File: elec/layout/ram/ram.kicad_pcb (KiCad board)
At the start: 2 copper layers, 40 x 40 mm, 56 parts, among them U1 _NXP_Semicon_MIMX8MM6CVTKZAA

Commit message: Building! started on layout
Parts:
- removed C37, C48: 10µF ±20% 6.3V X5R, lcsc:C0402
- removed C38, C39, C40, C41, C42, C43, C50, C51, C52, C53, C54: 1µF ±20% 6.3V X5R, lcsc:C0201
- removed C44, C46, C47, C55: 220nF ±20% 6.3V X5R, lcsc:C0201
- removed C45: 2.2µF ±20% 6.3V X5R, lcsc:C0402
- removed C49: 4.7µF ±20% 10V X5R, lcsc:C0402
- C1: value 2.2µF ±20% 6.3V X5R -> 10µF ±20% 6.3V X5R; footprint lcsc:C0201 -> lcsc:C0402; moved to B.Cu
- C10, C11, C13, C16, C17, C24, C26, C27, C28, C30: moved to B.Cu
- C12, C14, C32, C33, C34, C35, C4, C5, C6, C7, C8, C9: value 1µF ±20% 6.3V X5R -> 220nF ±20% 6.3V X5R; moved to B.Cu
- C15, C2, C3, C36: value 10µF ±20% 6.3V X5R -> 220nF ±20% 6.3V X5R; footprint lcsc:C0402 -> lcsc:C0201; moved to B.Cu
- C18, C19, C20, C21, C22, C23, C29: value 220nF ±20% 6.3V X5R -> 10µF ±20% 6.3V X5R; footprint lcsc:C0201 -> lcsc:C0402; moved to B.Cu
- C25: value 4.7µF ±20% 10V X5R -> 10µF ±20% 6.3V X5R; moved to B.Cu
- C31: value 1µF ±20% 6.3V X5R -> 10µF ±20% 6.3V X5R; footprint lcsc:C0201 -> lcsc:C0402; moved to B.Cu
- U1: value _NXP_Semicon_MIMX8MM6CVTKZAA -> _SK_HYNIX_H9HCNNNBKUMLXR_NEE; footprint lcsc:BGA-486_L14.0-W14.0-P0.50-TL_NXP_MIMX8MMXDVTLZXA -> lcsc:FBGA-200_L15.0-W10.0-BL_H9HCNNNBKUMLXR
- moved C13 188.4 mm to (161.6, 96.9)
- moved C12 187.3 mm to (161.6, 94.8)
- moved C6 186.4 mm to (158.8, 97.7), turned to 180 degrees
- moved C11 186.2 mm to (161.6, 92.6)
- moved C5 185.4 mm to (158.8, 95.8), turned to 180 degrees
- moved C1 185.2 mm to (161.6, 90.5), turned to 180 degrees
- moved C4 184.4 mm to (158.8, 93.8), turned to 180 degrees
- moved C3 183.5 mm to (158.8, 91.9), turned to 180 degrees
- moved C2 182.5 mm to (158.8, 90.0), turned to 180 degrees
- moved C20 181.9 mm to (152.7, 98.8), turned to 180 degrees
- moved C27 181.5 mm to (152.7, 98.1), turned to 180 degrees
- moved C24 179.8 mm to (152.4, 95.4), turned to 90 degrees
- moved C26 178.1 mm to (152.4, 92.2), turned to -90 degrees
- moved C35 177.0 mm to (152.7, 89.4), turned to 180 degrees
- moved U1 176.4 mm to (149.5, 93.8)
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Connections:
- net dram_ac00 renamed signal-16
- net dram_ac03 renamed signal-14
- net dram_ac10 renamed signal-49
- net dram_ac23 renamed signal-25
- net dram_ac24 renamed signal-55
- net dram_ac32 renamed signal-28
- net dram_alert_n renamed signal-12
- net dram_dq00 renamed zq0
- net dram_dq07 renamed signal-53
- net dram_dq08 renamed signal-3
- net dram_dq11 renamed signal-0
- net dram_dq15 renamed signal-33
- net dram_dq17 renamed signal-5
- net dram_dq20 renamed signal-9
- net dram_dqs0_n renamed signal-34
- net dram_zn renamed signal-59
- net i2c1_scl renamed signal-24
- net i2c1_sda renamed signal-36
- net i2c2_scl renamed signal-57
- net i2c3_scl renamed signal-11
- net mipi_dsi_clk_p renamed signal-22
- net mipi_dsi_d0_p renamed signal-26
- net vdd_dram_pll_0p8 renamed ck_cb
- C1 pad 1: *BC98.processor-net-1 -> NVCC_DRAM_1V1
- C10 pad 1: NVCC_ENET -> NVCC_DRAM_1V1
- C11 pad 1: NVCC_SD2 -> NVCC_DRAM_1V1
- C12 pad 1: *BC98.processor-net-0 -> NVCC_DRAM_1V1
- C13 pad 1: VDDA_1V8 -> NVCC_DRAM_1V1
- C14 pad 1: VDDA_1V8 -> NVCC_DRAM_1V1
- C15 pad 1: VDDA_1V8 -> NVCC_DRAM_1V1
- C16 pad 1: VDDA_1V8 -> NVCC_DRAM_1V1
- C17 pad 1: VDDA_1V8 -> NVCC_DRAM_1V1
- C18 pad 1: VDDA_1V8 -> NVCC_DRAM_1V1
- C19 pad 1: VDDA_1V8 -> NVCC_DRAM_1V1
- C20 pad 1: VDDA_1V8 -> NVCC_DRAM_1V1
- C21 pad 1: VDDA_1V8 -> NVCC_DRAM_1V1
- C22 pad 1: VDDA_1V8 -> NVCC_DRAM_1V1
- C23 pad 1: VDDA_1V8 -> NVCC_DRAM_1V1
- C24 pad 1: VDDA_1V8 -> NVCC_DRAM_1V1
- C25 pad 1: VDD_3V3 -> VDD_1V8
- C26 pad 1: VDD_3V3 -> VDD_1V8
- C27 pad 1: VDD_3V3 -> VDD_1V8
- C28 pad 1: VDD_3V3 -> VDD_1V8
- C29 pad 1: VDD_3V3 -> VDD_1V8
- C30 pad 1: VDD_ARM_0V9 -> VDD_1V8
- C31 pad 1: VDD_ARM_0V9 -> VDD_1V8
- C32 pad 1: VDD_ARM_0V9 -> VDD_1V8
- C33 pad 1: VDD_ARM_0V9 -> VDD_1V8
- C34 pad 1: VDD_ARM_0V9 -> VDD_1V8
- C35 pad 1: VDD_ARM_0V9 -> VDD_1V8
- C36 pad 1: VDD_DRAM_0V9 -> VDD_1V8
- U1 pad A1: GND -> *5FE8.RAM.RAM-net-0
- U1 pad A10: mipi_dsi_d1_n -> GND
- U1 pad A11: mipi_dsi_clk_n -> *5FE8.RAM.RAM-net-0
- U1 pad A12: mipi_dsi_d2_n -> *5FE8.RAM.RAM-net-0
- U1 pad A2: dram_dqs0_p -> *5FE8.RAM.RAM-net-0
- U1 pad A3: dram_dq06 -> GND
- U1 pad A4: dram_dm0 -> NVCC_DRAM_1V1
- U1 pad A8: ecspi2_miso -> *5FE8.RAM.RAM-net-1
- U1 pad A9: mipi_dsi_d0_n -> NVCC_DRAM_1V1
- U1 pad AA1: dram_dqs2_p -> *5FE8.RAM.RAM-net-0
- U1 pad AA10: GND -> NVCC_DRAM_1V1
- U1 pad AA9: GND -> signal-42
- U1 pad AB1: dram_dm2 -> *5FE8.RAM.RAM-net-0
- U1 pad AB10: gpio1_io12 -> GND
- U1 pad AB2: dram_dq16 -> *5FE8.RAM.RAM-net-0
- U1 pad AB4: dram_ac20 -> NVCC_DRAM_1V1
- U1 pad AB5: dram_ac21 -> GND
- U1 pad AB9: gpio1_io15 -> NVCC_DRAM_1V1
- U1 pad B1: dram_dq05 -> *5FE8.RAM.RAM-net-0
- U1 pad B10: mipi_dsi_d1_p -> NVCC_DRAM_1V1
- U1 pad B12: mipi_dsi_d2_p -> *5FE8.RAM.RAM-net-0
- U1 pad B3: GND -> NVCC_DRAM_1V1
- U1 pad B5: dram_dq01 -> NVCC_DRAM_1V1
- U1 pad B8: ecspi2_mosi -> NVCC_DRAM_1V1
- U1 pad C1: dram_dq04 -> GND
- U1 pad C10: GND -> signal-38
- U1 pad C2: GND -> signal-4
- U1 pad C9: GND -> signal-39
- U1 pad D1: dram_dq03 -> NVCC_DRAM_1V1
- U1 pad D2: dram_dq02 -> GND
- U1 pad D5: dram_ac11 -> NVCC_DRAM_1V1
- U1 pad D9: i2c2_sda -> GND
- U1 pad E1: dram_dq14 -> GND
- U1 pad E3: GND -> signal-40
- U1 pad F1: dram_dm1 -> VDD_1V8
- U1 pad F10: i2c3_sda -> NVCC_DRAM_1V1
- U1 pad F3: GND -> NVCC_DRAM_1V1
- U1 pad F5: dram_ac01 -> NVCC_DRAM_1V1
- U1 pad G1: dram_dqs1_p -> GND
- U1 pad G2: dram_dq09 -> NVCC_DRAM_1V1
- U1 pad G9: GND -> VDD_1V8
- U1 pad H1: dram_dqs1_n -> NVCC_DRAM_1V1
- U1 pad H10: VDD_3V3 -> signal-7
- U1 pad H2: GND -> signal-31
- U1 pad J1: dram_dq10 -> GND
- U1 pad J10: VDD_DRAM_0V9 -> GND
- U1 pad J11: VDDA_1V8 -> signal-43
- U1 pad J12: VDDA_1V8 -> GND
- U1 pad J5: dram_ac07 -> *5FE8.RAM.RAM-net-1
- U1 pad K1: dram_dq13 -> NVCC_DRAM_1V1
- U1 pad K12: VDD_DRAM_0V9 -> NVCC_DRAM_1V1
- U1 pad K2: dram_dq12 -> GND
- U1 pad K3: GND -> NVCC_DRAM_1V1
- U1 pad K4: dram_ac02 -> GND
- U1 pad K5: dram_ac14 -> *5FE8.RAM.RAM-net-1
- U1 pad K8: NVCC_DRAM_1V1 -> *5FE8.RAM.RAM-net-1
- U1 pad K9: NVCC_DRAM_1V1 -> GND
- U1 pad N1: dram_ac26 -> NVCC_DRAM_1V1
- U1 pad N10: VDD_DRAM_0V9 -> NVCC_DRAM_1V1
- U1 pad N11: VDD_DRAM_0V9 -> GND
- U1 pad N12: GND -> NVCC_DRAM_1V1
- U1 pad N2: dram_ac19 -> GND
- U1 pad N3: GND -> NVCC_DRAM_1V1
- U1 pad N4: dram_ac12 -> GND
- U1 pad N5: dram_ac13 -> *5FE8.RAM.RAM-net-1
- U1 pad N8: NVCC_DRAM_1V1 -> *5FE8.RAM.RAM-net-1
- U1 pad N9: NVCC_DRAM_1V1 -> GND
- U1 pad P1: dram_vref -> GND
- U1 pad P12: VDD_DRAM_0V9 -> GND
- U1 pad P5: VDD_DRAM_0V9 -> *5FE8.RAM.RAM-net-1
- U1 pad R1: dram_reset_n -> NVCC_DRAM_1V1
- U1 pad R10: VDD_DRAM_0V9 -> signal-50
- U1 pad R11: VDD_DRAM_0V9 -> signal-58
- U1 pad R12: GND -> NVCC_DRAM_1V1
- U1 pad R3: GND -> *5FE8.RAM.RAM-net-1
- U1 pad R5: dram_ac33 -> NVCC_DRAM_1V1
- U1 pad R9: NVCC_DRAM_1V1 -> signal-52
- U1 pad T1: dram_ac234 -> GND
- U1 pad T2: dram_ac35 -> NVCC_DRAM_1V1
- U1 pad T9: NVCC_DRAM_1V1 -> VDD_1V8
- U1 pad U1: dram_ac25 -> VDD_1V8
- U1 pad U10: VDD_DRAM_0V9 -> NVCC_DRAM_1V1
- U1 pad U11: VDD_DRAM_0V9 -> signal-37
- U1 pad U12: GND -> VDD_1V8
- U1 pad U9: NVCC_DRAM_1V1 -> signal-32
- U1 pad V1: dram_dq21 -> GND
- U1 pad V12: VDD_DRAM_0V9 -> GND
- U1 pad V3: GND -> signal-18
- U1 pad V5: dram_ac36 -> GND
- U1 pad V8: NVCC_DRAM_1V1 -> GND
- U1 pad V9: NVCC_DRAM_1V1 -> signal-47
- U1 pad W1: dram_dq18 -> NVCC_DRAM_1V1
- U1 pad W10: VDD_DRAM_0V9 -> signal-15
- U1 pad W11: VDD_DRAM_0V9 -> GND
- U1 pad W12: VDDA_1V8 -> NVCC_DRAM_1V1
- U1 pad W2: dram_dq19 -> GND
- U1 pad W3: GND -> signal-44
- U1 pad W4: dram_ac22 -> GND
- U1 pad W5: dram_ac37 -> NVCC_DRAM_1V1
- U1 pad Y1: dram_dqs2_n -> GND
- U1 pad Y10: VDD_3V3 -> signal-29
- U1 pad Y2: GND -> signal-54
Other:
- board outline removed

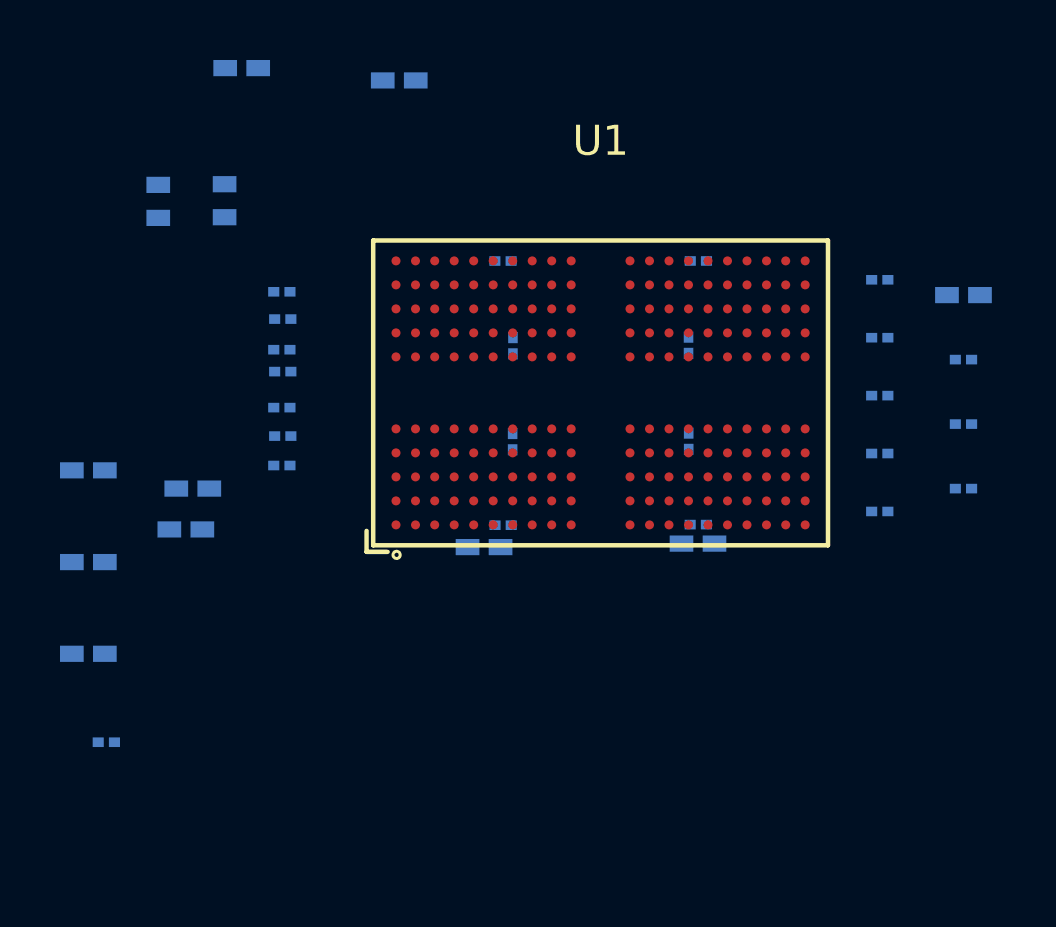
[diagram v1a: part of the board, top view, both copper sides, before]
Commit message: layout of capacitors for RAM chip
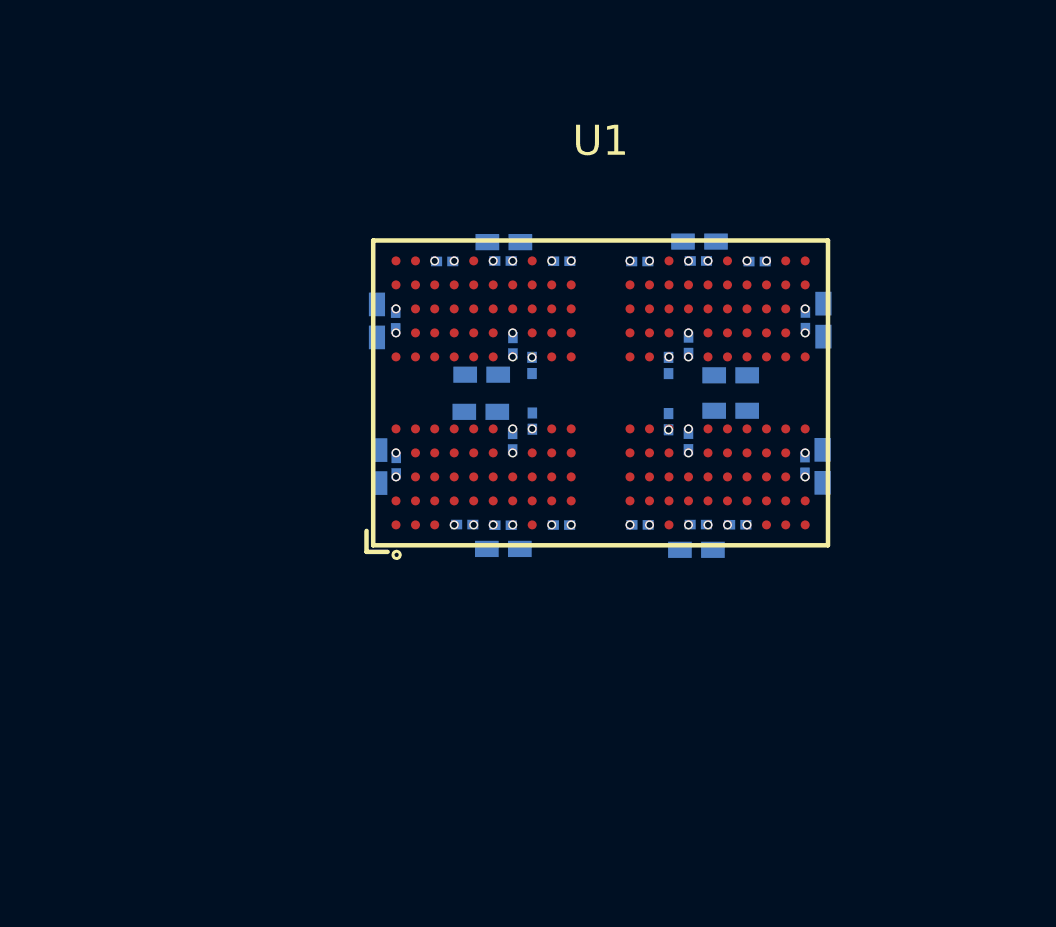
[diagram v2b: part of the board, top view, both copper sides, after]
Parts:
- moved C29 24.6 mm to (152.8, 88.7)
- moved C36 21.8 mm to (152.4, 95.4), turned to 90 degrees
- moved C21 21.1 mm to (156.9, 91.3), turned to 90 degrees
- moved C17 21.0 mm to (156.9, 96.2), turned to -90 degrees
- moved C30 20.3 mm to (152.7, 99.0)
- moved C31 14.1 mm to (146.2, 99.0), turned to 0 degrees
- moved C25 11.6 mm to (146.3, 88.7), turned to 0 degrees
- moved C23 10.3 mm to (145.5, 93.1), turned to 180 degrees
- moved C12 9.83 mm to (151.7, 94.7), turned to 90 degrees
- moved C7 9.39 mm to (148.2, 89.4)
- moved C16 8.33 mm to (147.2, 94.7), turned to 90 degrees
- moved C15 8.31 mm to (147.2, 92.8), turned to -90 degrees
- moved C1 8.21 mm to (153.8, 93.2), turned to 0 degrees
- moved C22 8.05 mm to (142.0, 91.4), turned to 90 degrees
- moved C2 8.02 mm to (150.8, 89.4), turned to 0 degrees
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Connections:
- net *5FE8.RAM-signal renamed reset
- net *5FE8.RAM.RAM-net-0 renamed *6228.RAM.RAM-net-0
- net *5FE8.RAM.RAM-net-1 renamed *6228.RAM.RAM-net-1
- U1 pad AA11: signal-51 -> signal-45
- U1 pad AA2: signal-5 -> signal-0
- U1 pad AA4: signal-21 -> signal-16
- U1 pad AA9: signal-42 -> signal-34
- U1 pad B11: signal-22 -> signal-17
- U1 pad B2: signal-34 -> signal-43
- U1 pad B4: signal-53 -> signal-58
- U1 pad B9: signal-26 -> signal-22
- U1 pad C10: signal-38 -> signal-32
- U1 pad C11: signal-48 -> signal-44
- U1 pad C2: signal-4 -> signal-59
- U1 pad C3: signal-10 -> signal-4
- U1 pad C4: signal-19 -> signal-14
- U1 pad C9: signal-39 -> signal-33
- U1 pad D10: signal-57 -> signal-50
- U1 pad D3: signal-27 -> signal-23
- U1 pad E10: signal-11 -> signal-5
- U1 pad E11: signal-20 -> signal-29
- U1 pad E2: signal-33 -> signal-38
- U1 pad E3: signal-40 -> signal-47
- U1 pad E4: signal-49 -> signal-55
- U1 pad E9: signal-24 -> signal-20
- U1 pad F11: signal-45 -> signal-39
- U1 pad F2: signal-3 -> signal-56
- U1 pad F4: signal-16 -> signal-11
- U1 pad F9: signal-36 -> signal-31
- U1 pad H10: signal-7 -> signal-18
- U1 pad H11: signal-17 -> signal-28
- U1 pad H2: signal-31 -> signal-37
- U1 pad H4: signal-1 -> signal-54
- U1 pad H9: signal-23 -> signal-19
- U1 pad J11: signal-43 -> signal-36
- U1 pad J2: signal-0 -> signal-53
- U1 pad J4: signal-14 -> signal-10
- U1 pad P11: signal-41 -> signal-52
- U1 pad P2: signal-59 -> signal-8
- U1 pad P4: signal-13 -> signal-26
- U1 pad R10: signal-50 -> signal-2
- U1 pad R11: signal-58 -> signal-9
- U1 pad R2: signal-12 -> signal-27
- U1 pad R4: signal-28 -> signal-35
- U1 pad R9: signal-52 -> signal-15
- U1 pad U11: signal-37 -> signal-51
- U1 pad U2: signal-55 -> signal-6
- U1 pad U4: signal-8 -> signal-24
- U1 pad U9: signal-32 -> signal-46
- U1 pad V10: signal-46 -> signal-1
- U1 pad V11: signal-56 -> signal-7
- U1 pad V2: signal-9 -> signal-25
- U1 pad V3: signal-18 -> signal-40
- U1 pad V4: signal-25 -> signal-48
- U1 pad V9: signal-47 -> signal-12
- U1 pad W10: signal-15 -> signal-30
- U1 pad W3: signal-44 -> signal-57
- U1 pad Y10: signal-29 -> signal-41
- U1 pad Y11: signal-35 -> signal-49
- U1 pad Y2: signal-54 -> signal-3
- U1 pad Y3: signal-2 -> signal-13
- U1 pad Y4: signal-6 -> signal-21
- U1 pad Y9: signal-30 -> signal-42
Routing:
- net VDD_1V8: vias 0 -> 8
- net NVCC_DRAM_1V1: vias 0 -> 16
- net GND: vias 0 -> 20

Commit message: Update ato.yaml to build nonos + import into layout
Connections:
- net *6228.RAM.RAM-net-0 renamed *D4A8.RAM-net-1
- net *6228.RAM.RAM-net-1 renamed *D4A8.RAM-net-0
- net GND renamed lv
- net NVCC_DRAM_1V1 renamed hv
- net VDD_1V8 renamed *D4A8-net
- net signal-57 renamed dqs0_tb
- U1 pad AA11: signal-45 -> signal-2
- U1 pad AA2: signal-0 -> signal-35
- U1 pad AA4: signal-16 -> signal-55
- U1 pad AA9: signal-34 -> signal-45
- U1 pad B11: signal-17 -> signal-5
- U1 pad B2: signal-43 -> signal-18
- U1 pad B4: signal-58 -> signal-33
- U1 pad B9: signal-22 -> signal-56
- U1 pad C10: signal-32 -> signal-9
- U1 pad C11: signal-44 -> signal-19
- U1 pad C2: signal-59 -> signal-34
- U1 pad C3: signal-4 -> signal-41
- U1 pad C4: signal-14 -> signal-6
- U1 pad C9: signal-33 -> signal-23
- U1 pad D10: signal-50 -> dqs1_ta
- U1 pad D3: signal-23 -> dqs0_ta
- U1 pad E10: signal-5 -> signal-51
- U1 pad E11: signal-29 -> signal-4
- U1 pad E2: signal-38 -> signal-16
- U1 pad E3: signal-47 -> signal-24
- U1 pad E4: signal-55 -> signal-29
- U1 pad E9: signal-20 -> signal-52
- U1 pad F11: signal-39 -> signal-17
- U1 pad F2: signal-56 -> signal-30
- U1 pad F4: signal-11 -> signal-44
- U1 pad F9: signal-31 -> signal-21
- U1 pad H10: signal-18 -> signal-47
- U1 pad H11: signal-28 -> signal-1
- U1 pad H2: signal-37 -> signal-14
- U1 pad H4: signal-54 -> signal-26
- U1 pad H9: signal-19 -> signal-48
- U1 pad J11: signal-36 -> signal-11
- U1 pad J2: signal-53 -> signal-25
- U1 pad J4: signal-10 -> signal-0
- U1 pad P11: signal-52 -> signal-10
- U1 pad P2: signal-8 -> signal-39
- U1 pad P4: signal-26 -> signal-53
- U1 pad R10: signal-2 -> signal-32
- U1 pad R11: signal-9 -> signal-40
- U1 pad R2: signal-27 -> signal-54
- U1 pad R4: signal-35 -> signal-8
- U1 pad R9: signal-15 -> signal-31
- U1 pad U11: signal-51 -> signal-22
- U1 pad U2: signal-6 -> signal-37
- U1 pad U4: signal-24 -> signal-49
- U1 pad U9: signal-46 -> signal-15
- U1 pad V10: signal-1 -> signal-27
- U1 pad V11: signal-7 -> signal-38
- U1 pad V2: signal-25 -> signal-50
- U1 pad V3: signal-40 -> signal-3
- U1 pad V4: signal-48 -> signal-7
- U1 pad V9: signal-12 -> signal-28
- U1 pad W10: signal-30 -> signal-43
- U1 pad Y10: signal-41 -> signal-12
- U1 pad Y11: signal-49 -> signal-20
- U1 pad Y2: signal-3 -> signal-36
- U1 pad Y3: signal-13 -> signal-42
- U1 pad Y4: signal-21 -> signal-46
- U1 pad Y9: signal-42 -> signal-13

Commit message: update naming
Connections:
- net *D4A8-net renamed *3278-net
- net *D4A8.RAM-net-0 renamed *3278.RAM-net-1
- net *D4A8.RAM-net-1 renamed *3278.RAM-net-0
- U1 pad AA11: signal-2 -> signal-20
- U1 pad AA2: signal-35 -> signal-12
- U1 pad AA4: signal-55 -> signal-19
- U1 pad AA9: signal-45 -> signal-0
- U1 pad B11: signal-5 -> signal-54
- U1 pad B2: signal-18 -> signal-17
- U1 pad B9: signal-56 -> signal-49
- U1 pad C10: signal-9 -> signal-8
- U1 pad C11: signal-19 -> signal-18
- U1 pad C3: signal-41 -> signal-39
- U1 pad C4: signal-6 -> signal-44
- U1 pad C9: signal-23 -> signal-9
- U1 pad D3: dqs0_ta -> signal-50
- U1 pad E10: signal-51 -> dqs1_ca
- U1 pad E11: signal-4 -> signal-53
- U1 pad E2: signal-16 -> signal-15
- U1 pad E3: signal-24 -> dqs0_ca
- U1 pad E9: signal-52 -> signal-47
- U1 pad F11: signal-17 -> signal-16
- U1 pad F4: signal-44 -> signal-43
- U1 pad F9: signal-21 -> signal-3
- U1 pad H10: signal-47 -> signal-4
- U1 pad H11: signal-1 -> signal-10
- U1 pad H2: signal-14 -> signal-24
- U1 pad H4: signal-26 -> signal-45
- U1 pad H9: signal-48 -> signal-5
- U1 pad J11: signal-11 -> signal-25
- U1 pad J2: signal-25 -> signal-41
- U1 pad J4: signal-0 -> signal-51
- U1 pad P11: signal-10 -> signal-11
- U1 pad P2: signal-39 -> signal-23
- U1 pad P4: signal-53 -> signal-40
- U1 pad R10: signal-32 -> signal-31
- U1 pad R11: signal-40 -> signal-37
- U1 pad R2: signal-54 -> signal-48
- U1 pad R4: signal-8 -> signal-6
- U1 pad R9: signal-31 -> signal-32
- U1 pad U11: signal-22 -> signal-7
- U1 pad U2: signal-37 -> signal-22
- U1 pad U4: signal-49 -> signal-38
- U1 pad U9: signal-15 -> signal-14
- U1 pad V10: signal-27 -> signal-26
- U1 pad V11: signal-38 -> signal-35
- U1 pad V2: signal-50 -> signal-46
- U1 pad V3: signal-3 -> dqs0_cb
- U1 pad V4: signal-7 -> signal-1
- U1 pad V9: signal-28 -> signal-27
- U1 pad W10: signal-43 -> signal-42
- U1 pad Y10: signal-12 -> signal-52
- U1 pad Y11: signal-20 -> signal-2
- U1 pad Y2: signal-36 -> signal-21
- U1 pad Y3: signal-42 -> signal-28
- U1 pad Y4: signal-46 -> signal-36
